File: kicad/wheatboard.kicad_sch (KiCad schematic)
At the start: 0 parts

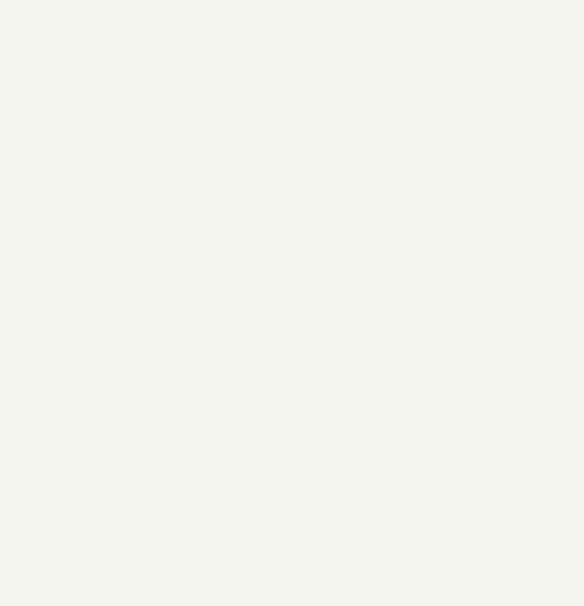
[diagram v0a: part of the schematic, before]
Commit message: actual attempt at source controlling kicad project
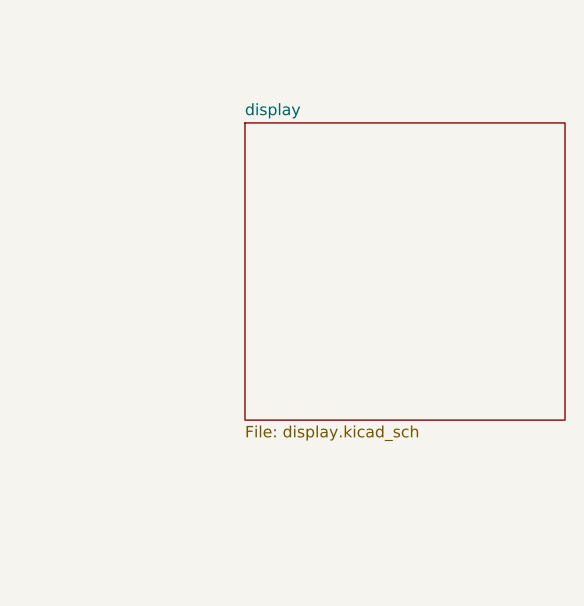
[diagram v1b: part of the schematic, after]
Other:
- added sheet display (display.kicad_sch)
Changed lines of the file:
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@@
 (kicad_sch
-	(version 20231120)
+	(version 20250114)
 	(generator "eeschema")
-	(generator_version "8.0")
+	(generator_version "9.0")
 	(paper "A4")
 	(sheet
 		(at 40.64 121.92)
 		(size 36.83 25.4)
+		(exclude_from_sim no)
+		(in_bom yes)
+		(on_board yes)
+		(dnp no)
 		(fields_autoplaced yes)
 		(stroke
@@
 		)
 		(instances
-			(project "keyboard"
+			(project "wheatboard"
 				(path "/6dbb65f4-5576-4e18-9627-83014d84ecc4"
 					(page "4")
@@
 		(at 40.64 36.83)
 		(size 36.83 25.4)
+		(exclude_from_sim no)
+		(in_bom yes)
+		(on_board yes)
+		(dnp no)
 		(fields_autoplaced yes)
 		(stroke
@@
 		)
 		(instances
-			(project "keyboard"
+			(project "wheatboard"
 				(path "/6dbb65f4-5576-4e18-9627-83014d84ecc4"
 					(page "2")
@@
 		(at 116.84 40.64)
 		(size 64.77 63.5)
+		(exclude_from_sim no)
+		(in_bom yes)
+		(on_board yes)
+		(dnp no)
 		(fields_autoplaced yes)
 		(stroke
@@
 		)
 		(instances
-			(project "keyboard"
+			(project "wheatboard"
 				(path "/6dbb65f4-5576-4e18-9627-83014d84ecc4"
 					(page "5")
@@
 		(at 40.64 81.28)
 		(size 36.83 24.13)
+		(exclude_from_sim no)
+		(in_bom yes)
+		(on_board yes)
+		(dnp no)
 		(fields_autoplaced yes)
 		(stroke
@@
 		)
 		(instances
-			(project "keyboard"
+			(project "wheatboard"
 				(path "/6dbb65f4-5576-4e18-9627-83014d84ecc4"
 					(page "3")
@@
 		(at 118.11 129.54)
 		(size 39.37 34.29)
+		(exclude_from_sim no)
+		(in_bom yes)
+		(on_board yes)
+		(dnp no)
 		(fields_autoplaced yes)
 		(stroke
@@
 		)
 		(instances
-			(project "keyboard"
+			(project "wheatboard"
 				(path "/6dbb65f4-5576-4e18-9627-83014d84ecc4"
 					(page "6")
+				)
+			)
+		)
+	)
+	(sheet
+		(at 211.455 45.72)
+		(size 35.56 33.02)
+		(exclude_from_sim no)
+		(in_bom yes)
+		(on_board yes)
+		(dnp no)
+		(fields_autoplaced yes)
+		(stroke
+			(width 0.1524)
+			(type solid)
+		)
+		(fill
+			(color 0 0 0 0.0000)
+		)
+		(property "Sheetname" "display"
+			(at 211.455 45.0084 0)
+			(effects
+				(font
+					(size 1.27 1.27)
+				)
+				(justify left bottom)
+			)
+		)
+		(property "Sheetfile" "display.kicad_sch"
+			(at 211.455 79.3246 0)
+			(effects
+				(font
+					(size 1.27 1.27)
+				)
+				(justify left top)
+			)
+		)
+		(instances
+			(project "wheatboard"
+				(path "/6dbb65f4-5576-4e18-9627-83014d84ecc4"
+					(page "7")
 				)
 			)
@@
 		)
 	)
+	(embedded_fonts no)
 )
